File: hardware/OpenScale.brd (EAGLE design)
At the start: 54.6 x 40.6 mm, 59 parts, among them Q1 200mA/50V, Q2 200mA/50V, U1 HX711, U3 TMP102, U4 ATMEGA328P_TQFP, U5 MIC52055-5V, U6 FT231X, Y2 16MHZ

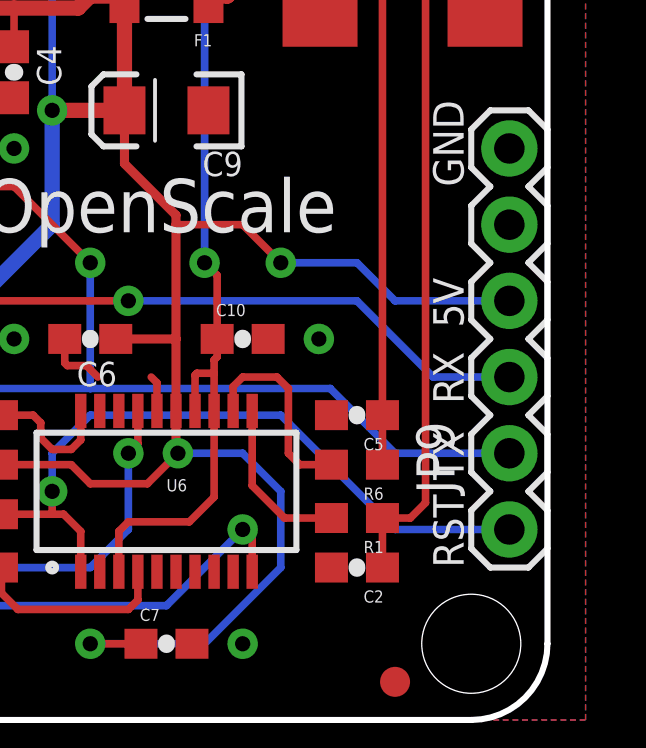
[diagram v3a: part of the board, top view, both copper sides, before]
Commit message: Adding support for temperature readings.
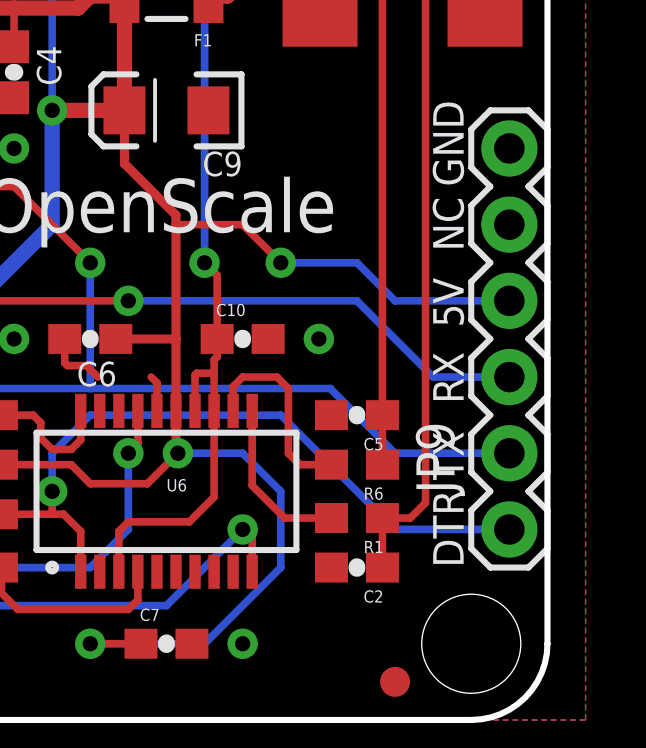
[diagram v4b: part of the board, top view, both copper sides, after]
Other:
- board text added: "DAT"
- board text added: "DTR"
- board text added: "NC"
- board text removed: "RST"
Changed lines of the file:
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@@
 <text x="8.255" y="36.195" size="1.27" layer="21" font="vector" ratio="15">Ext Temp</text>
 <text x="10.795" y="37.592" size="1.27" layer="22" font="vector" ratio="15" rot="MR270">5V</text>
-<text x="13.335" y="37.592" size="1.27" layer="22" font="vector" ratio="15" rot="MR270">SIG</text>
+<text x="13.335" y="37.592" size="1.27" layer="22" font="vector" ratio="15" rot="MR270">DAT</text>
 <text x="15.875" y="37.592" size="1.27" layer="22" font="vector" ratio="15" rot="MR270">GND</text>
 <text x="38.1" y="34.798" size="1.27" layer="21" font="vector" ratio="15">Reset</text>
@@
 <text x="9.271" y="0.635" size="1.27" layer="21" font="vector" ratio="15">B-</text>
 <wire x1="27.305" y1="41.402" x2="27.305" y2="-0.889" width="0.254" layer="51"/>
-<text x="51.816" y="5.08" size="1.016" layer="21" font="vector" ratio="15" rot="R90">RST</text>
-<text x="50.8" y="5.08" size="1.016" layer="22" font="vector" ratio="15" rot="MR90">RST</text>
+<text x="51.816" y="5.08" size="1.016" layer="21" font="vector" ratio="15" rot="R90">DTR</text>
+<text x="50.8" y="5.08" size="1.016" layer="22" font="vector" ratio="15" rot="MR90">DTR</text>
 <text x="49.911" y="15.875" size="1.778" layer="22" font="vector" ratio="15" rot="MR270">FTDI</text>
 <text x="49.53" y="17.78" size="1.016" layer="22" font="vector" ratio="15" rot="MR90">BLK</text>
@@
 <text x="12.573" y="30.48" size="1.27" layer="22" font="vector" ratio="15" rot="MR180">SIG</text>
 <rectangle x1="27.559" y1="35.941" x2="28.321" y2="37.719" layer="41"/>
+<text x="51.816" y="15.621" size="1.016" layer="21" font="vector" ratio="15" rot="R90">NC</text>
+<text x="50.8" y="15.621" size="1.016" layer="22" font="vector" ratio="15" rot="MR90">NC</text>
+<text x="7.493" y="30.48" size="1.27" layer="22" font="vector" ratio="15" rot="MR0">GND</text>
 </plain>
 <attributes>

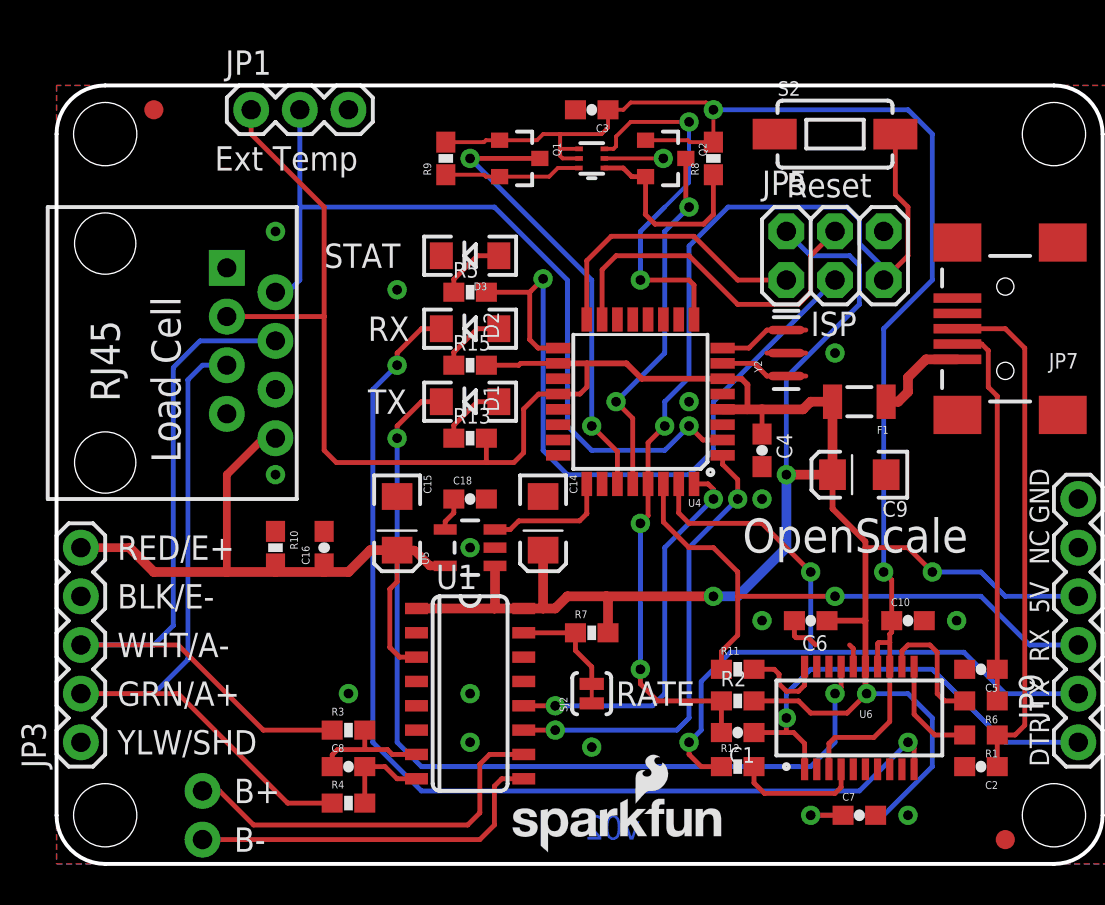
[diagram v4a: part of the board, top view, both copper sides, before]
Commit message: Remove v-reg add PNP for internal v-reg.
Added 4.7k pull up for One Wire external temp.
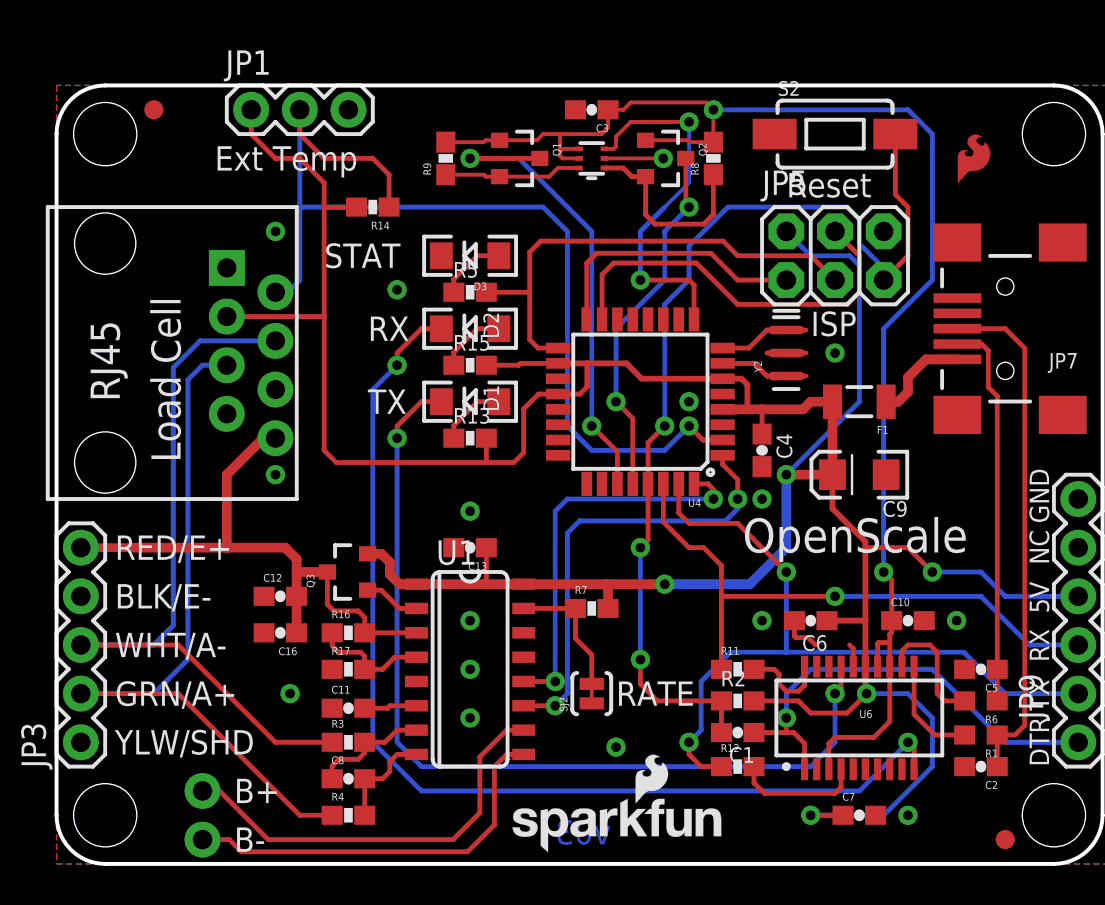
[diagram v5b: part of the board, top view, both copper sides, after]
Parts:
- removed C14, C15: 10uF, SparkFun-Capacitors:EIA3216
- removed C18: 470pF, SparkFun-Capacitors:0603-CAP
- removed R10: 100, SparkFun-Resistors:0603-RES
- removed U5: MIC52055-5V, SparkFun-PowerIC:SOT23-5
- added C11: 0.1uF, SparkFun-Capacitors:0603-CAP
- added C12, C13: 1.0uF, SparkFun-Capacitors:0603-CAP
- added LOGO3: SFE_LOGO_FLAME.1EXP, SparkFun-Aesthetics:SFE_LOGO_FLAME_COPPER_EXPOSED_.1
- added Q3: MMBT4403, SparkFun-DiscreteSemi:SOT23-3
- added R14: 4.7K, SparkFun-Resistors:0603-RES
- added R16: 20K, SparkFun-Resistors:0603-RES
- added R17: 8.2K, SparkFun-Resistors:0603-RES
- moved C16 5.00 mm to (11.7, 12.1), turned to 180 degrees
- moved R7 1.27 mm to (27.9, 13.3)
- moved U1 1.27 mm to (21.6, 10.2)
- moved R3 0.64 mm to (15.2, 6.35)
- moved C8 0.63 mm to (15.2, 4.45)
- moved R4 0.63 mm to (15.2, 2.54)
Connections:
- removed net AMP_EN: U4.25, U5.3
- removed net N$15: C18.1, U5.4
- new net N$17: Q3.1, U1.2
- new net N$18: R16.1, R17.2, U1.4
- new net N$21: C11.2, U1.6
- net 5V: now also C13.1, Q3.2, R14.2; no longer C14.A, U5.1
- net AVDD: now also C12.2, Q3.3, R16.2; no longer C15.A, R10.2, U5.5
- net GND: now also C11.1, C12.1, C13.2, R17.1; no longer C14.C, C15.C, C18.2, R10.1, U1.4, U5.2
- net TEMP_DAT: now also R14.1
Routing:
- net D13: track 37.8 -> 25.5 mm, vias 1 -> 0
- net TEMP_DAT: track 43.0 -> 53.0 mm
- net AMP_EN: track 6.69 -> 0.00 mm
- net N$18: track 0.00 -> 6.24 mm
- net AVDD: track 36.4 -> 31.6 mm
- net N$17: track 0.00 -> 2.95 mm
- net N$21: track 0.00 -> 2.75 mm
- net D11: track 18.8 -> 20.9 mm
- net N$15: track 1.78 -> 0.00 mm
- net B-: track 19.3 -> 20.9 mm
- net 5V: track 170.1 -> 171.6 mm
- net SDA: track 23.8 -> 25.3 mm
- net B+: track 20.5 -> 21.9 mm
- net N$9: track 5.72 -> 6.99 mm
- net TXD: track 41.1 -> 39.8 mm
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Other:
- board text added: "v03"

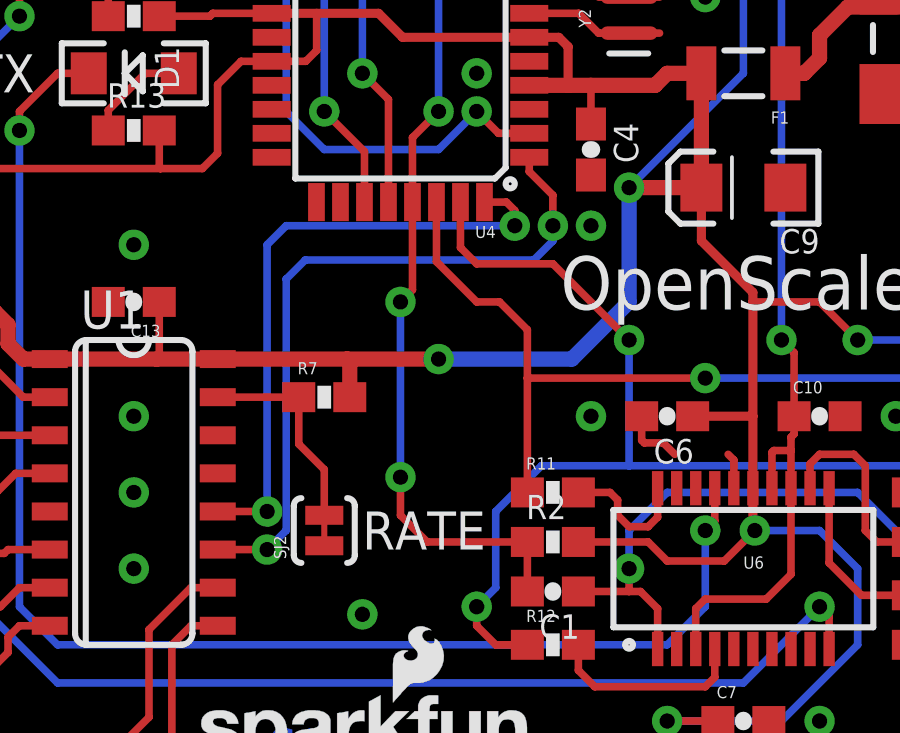
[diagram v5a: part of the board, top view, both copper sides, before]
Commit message: Fixed issue 4 - DRC errors and schematic markings.
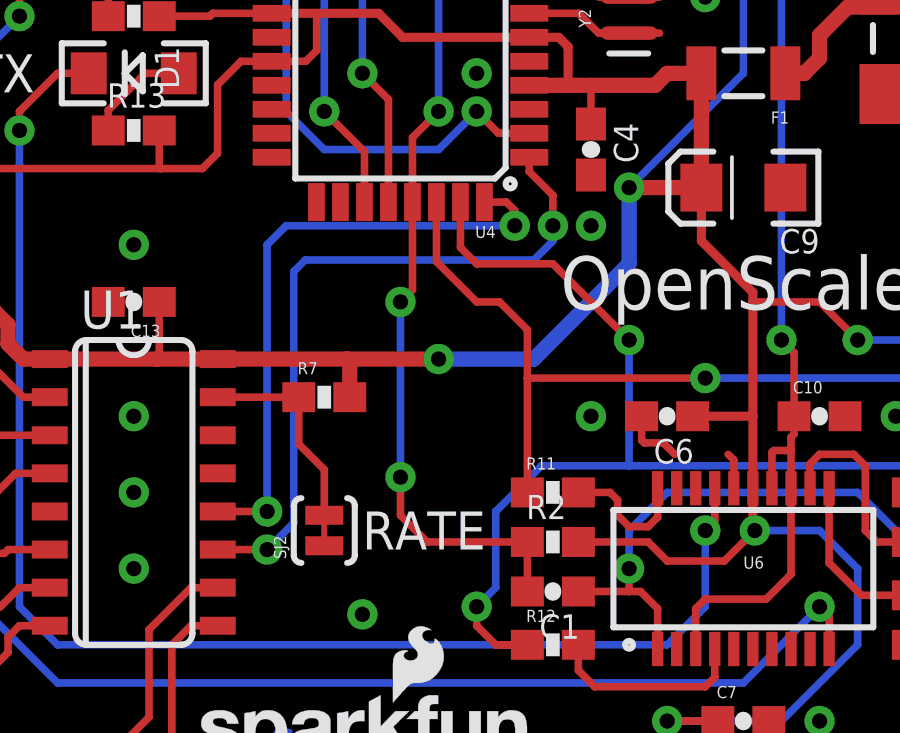
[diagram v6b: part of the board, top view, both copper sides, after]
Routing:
- net 5V: track 171.6 -> 170.8 mm
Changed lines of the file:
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@@
 <layer number="47" name="Measures" color="7" fill="1" visible="no" active="yes"/>
 <layer number="48" name="Document" color="7" fill="1" visible="no" active="yes"/>
-<layer number="49" name="Reference" color="7" fill="1" visible="yes" active="yes"/>
+<layer number="49" name="Reference" color="7" fill="1" visible="no" active="yes"/>
 <layer number="50" name="dxf" color="7" fill="1" visible="no" active="no"/>
 <layer number="51" name="tDocu" color="6" fill="1" visible="yes" active="yes"/>
@@
 <wire x1="10.16" y1="39.37" x2="10.16" y2="38.1" width="0.254" layer="1"/>
 <via x="31.75" y="14.605" extent="1-16" drill="0.508"/>
-<wire x1="31.75" y1="14.605" x2="36.195" y2="14.605" width="0.508" layer="16"/>
-<wire x1="36.195" y1="14.605" x2="38.1" y2="16.51" width="0.508" layer="16"/>
-<wire x1="38.1" y1="16.51" x2="38.1" y2="20.32" width="0.508" layer="16"/>
+<wire x1="31.75" y1="14.605" x2="34.925" y2="14.605" width="0.508" layer="16"/>
+<wire x1="34.925" y1="14.605" x2="38.1" y2="17.78" width="0.508" layer="16"/>
+<wire x1="38.1" y1="17.78" x2="38.1" y2="20.32" width="0.508" layer="16"/>
 <via x="38.1" y="20.32" extent="1-16" drill="0.508"/>
 <wire x1="24.384" y1="23.749" x2="24.384" y2="21.463" width="0.254" layer="1"/>
@@
 <wire x1="34.7726" y1="20.8534" x2="34.7726" y2="21.33" width="0.254" layer="1"/>
 <wire x1="24.39" y1="8.255" x2="26.035" y2="8.255" width="0.254" layer="1"/>
-<wire x1="26.035" y1="8.255" x2="26.67" y2="8.89" width="0.254" layer="16"/>
-<wire x1="26.67" y1="8.89" x2="26.67" y2="17.272" width="0.254" layer="16"/>
-<wire x1="26.67" y1="17.272" x2="27.305" y2="17.907" width="0.254" layer="16"/>
+<wire x1="26.035" y1="8.255" x2="26.924" y2="9.144" width="0.254" layer="16"/>
+<wire x1="26.924" y1="17.526" x2="27.305" y2="17.907" width="0.254" layer="16"/>
 <wire x1="27.305" y1="17.907" x2="34.925" y2="17.907" width="0.254" layer="16"/>
 <wire x1="34.925" y1="17.907" x2="35.56" y2="18.542" width="0.254" layer="16"/>
 <wire x1="35.56" y1="18.542" x2="35.56" y2="19.05" width="0.254" layer="16"/>
+<wire x1="26.924" y1="9.144" x2="26.924" y2="17.526" width="0.254" layer="16"/>
 </signal>
 <signal name="B-">

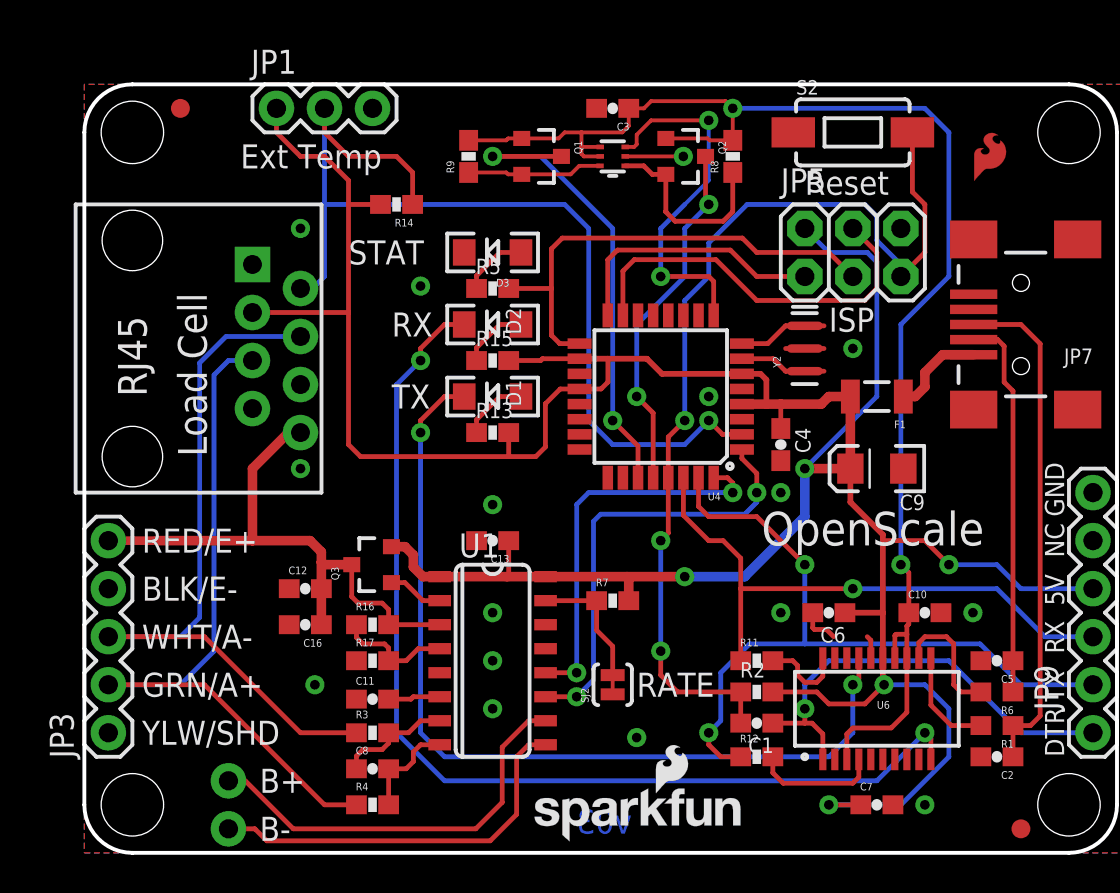
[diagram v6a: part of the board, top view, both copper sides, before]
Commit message: Crazy re-design to use screw terminals.
Rather than RJ45 I have moved to screw terminals. This should make it
easy on end customers who don't have a solder iron to get up and running
immediately.
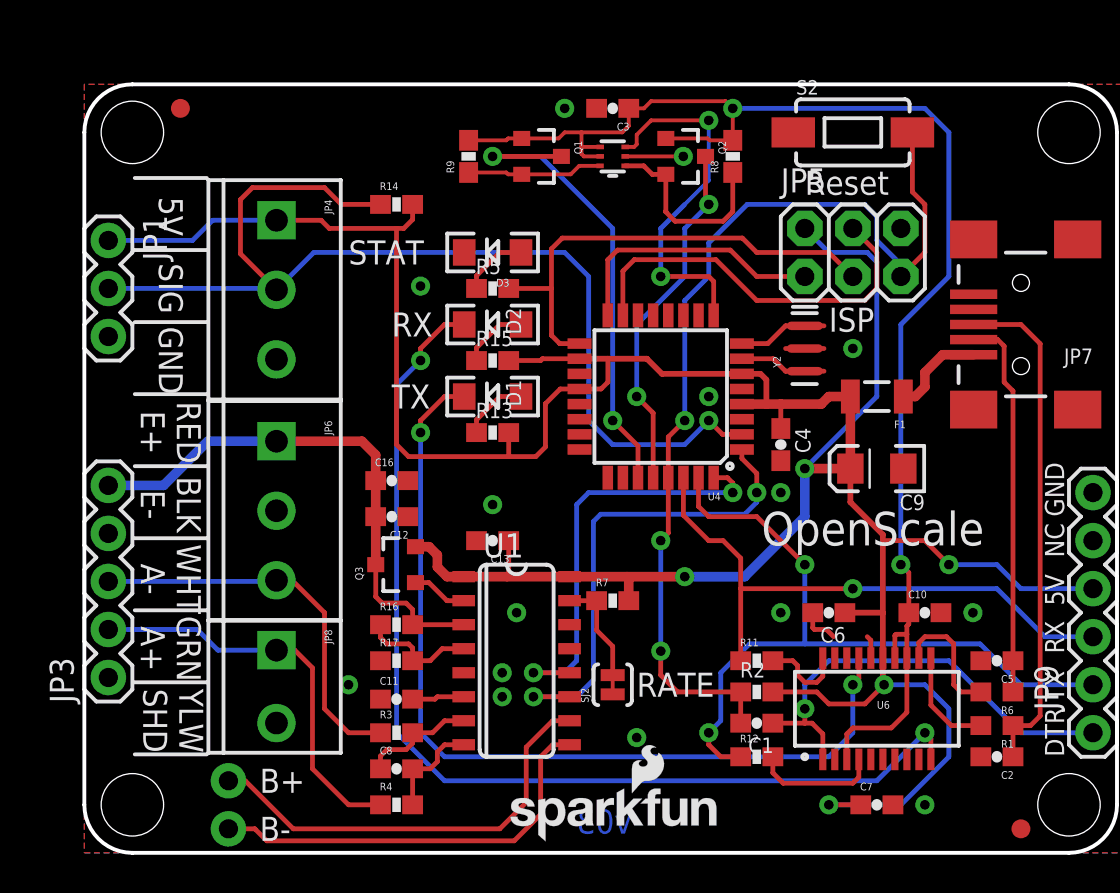
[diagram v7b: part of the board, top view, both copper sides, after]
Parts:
- added JP4: Screw, SparkFun-Connectors:SCREWTERMINAL-3.5MM-3_LOCK.007S
- added JP8: (no value), SparkFun-Connectors:SCREWTERMINAL-3.5MM-2_LOCK
- JP6: value RJ45 -> (none); device SparkFun-Connectors:RJ45-8 -> SparkFun-Connectors:SCREWTERMINAL-3.5MM-3_LOCK.007S
- LOGO3: value SFE_LOGO_FLAME.1EXP -> SFE_LOGO_FLAME.1_STOP; device SparkFun-Aesthetics:SFE_LOGO_FLAME_COPPER_EXPOSED_.1 -> SparkFun-Aesthetics:SFE_LOGO_FLAME_STOP_.1
- moved JP1 11.3 mm to (1.27, 32.4), turned to 270 degrees
- moved JP6 9.16 mm to (10.2, 21.6)
- moved C16 8.89 mm to (16.3, 19.7), turned to 0 degrees
- moved C12 5.95 mm to (16.3, 17.8), turned to 180 degrees
- moved JP3 2.92 mm to (1.27, 9.27)
- moved C11 1.27 mm to (16.5, 8.13)
- moved C8 1.27 mm to (16.5, 4.45)
- moved Q3 1.27 mm to (16.5, 15.2)
- moved R16 1.27 mm to (16.5, 12.1)
- moved R17 1.27 mm to (16.5, 10.2)
- moved R3 1.27 mm to (16.5, 6.35)
- moved R4 1.27 mm to (16.5, 2.54)
- moved LOGO1 1.27 mm to (22.1, 0.51)
- moved U1 1.27 mm to (22.9, 10.2)
- moved LOGO3 0.25 mm to (46.5, 35.2)
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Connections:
- net 5V: now also JP4.1; no longer JP6.3
- net A+: now also JP8.1; no longer JP6.5
- net A-: now also JP6.3; no longer JP6.4
- net AVDD: now also JP6.1; no longer JP6.8
- net GND: now also JP4.3, JP6.2, JP8.2; no longer JP6.1, JP6.6, JP6.7
- net TEMP_DAT: now also JP4.2; no longer JP6.2
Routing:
- net A-: track 39.8 -> 20.8 mm
- net A+: track 39.0 -> 21.4 mm
- net TEMP_DAT: track 53.0 -> 57.4 mm
- net AVDD: track 31.6 -> 28.6 mm
- net LC_SCK: track 23.5 -> 26.0 mm
- net LC_DOUT: track 21.2 -> 22.9 mm
- net 5V: track 170.8 -> 169.3 mm
- net N$9: track 6.99 -> 5.72 mm
- net B-: track 20.9 -> 22.2 mm
- net B+: track 21.9 -> 23.2 mm
- net GND: vias 16 -> 15
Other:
- board text added: "BLK E-"
- board text added: "GRN A+"
- board text added: "RED"
- board text added: "RED E+"
- board text added: "WHT"
- board text added: "WHT A-"
- board text added: "YLW"
- board text added: "YLW SHD"
- board text removed: "A+"
- board text removed: "A-"
- board text removed: "BLK/E-"
- board text removed: "DAT"
- board text removed: "E+"
- board text removed: "E-"
- board text removed: "GRN/A+"
- board text removed: "RED/E+"
- board text removed: "RJ45"
- board text removed: "SHD"
- board text removed: "WHT/A-"
- board text removed: "YLW/SHD"
